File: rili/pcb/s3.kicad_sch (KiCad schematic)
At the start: 91 parts, among them J2 Conn_02x03_Odd_Even, J20 TPS43_FPC, J4 AudioJack4, SW100 SW_PUSH, SW101 SW_PUSH, SW102 SW_PUSH, SW103 SW_PUSH, SW104 SW_PUSH, SW105 SW_PUSH, SW74 SW_PUSH, SW75 SW_PUSH, SW76 SW_PUSH, SW77 SW_PUSH, SW82 SW_PUSH, SW83 SW_PUSH, SW84 SW_PUSH, SW85 SW_PUSH, SW88 SW_PUSH, SW89 SW_PUSH, SW90 SW_PUSH, SW91 SW_PUSH, SW92 SW_PUSH, SW93 SW_PUSH, SW94 SW_PUSH, SW95 SW_PUSH, SW96 SW_PUSH, SW97 SW_PUSH, SW98 SW_PUSH, SW99 SW_PUSH, U1 ESP32-S3-WROOM-1, U10 SiP32431DR3, U13 D, U14 D, U8 NRF24L01_Breakout, U9 SRV05-4

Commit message: layout v2 : carte routée — PCB↔schéma réconciliés, BOM LCSC, TVS matrice, DRC 990→24
- réconciliation PCB↔schéma en une passe : 105 empreintes remariées (matrice ×2,
  module P4), 54 périmées supprimées, ~140 importées par F8 ; footprint TRRS
  MJ-4PP-9_rev3 créé (pads mappés de l'ancien design fonctionnel)
- placement : moitié droite générée au miroir exact du pré-placement gauche
  (axe x=188.46048), trous de montage symétrisés, origine de grille sur l'axe
- protection ESD matrice : 22 SD05C-01F (un par ligne, côté switchs des 100R,
  validés par partition de netlist) ; PWR_FLAG +5V_D réparé
- BOM LCSC dans les propriétés des symboles (32 composants : réfs, liens,
  notes d'achat) + annexe courses complète au plan v2 ; connecteur trackpad
  corrigé (ZIF Hirose FH12-6S-0.5SH, réf MNT Reform)
- règles JLCPCB (planchers DRC + classes Default/Power re-branchées v2),
  passage 4 couches, routage complet des deux moitiés
- gerbers v1 corne-cherry retirés (obsolètes)
- baselines tripwire re-référencées : DRC 990→24 erreurs / 208→17 warnings,
  ERC 0 erreur / 200 warnings (53 fantômes headless documentés)

Co-Authored-By: Claude Fable 5 <noreply@anthropic.com>
Claude-Session: https://claude.ai/code/session_01GfX5RmekmQi78Dm37qsT4Z
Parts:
- added D100, D101, D102, D103, D104, D105, D106, D107, D108, D109, D110: SD05C-01F, Diode_SMD:D_SOD-323, symbol Diode:SD05C-01F
- added H5, H6, H7, H8: MountingHole_Pad_MP, MountingHole:MountingHole_3.2mm_M3_DIN965_Pad, symbol Mechanical:MountingHole_Pad_MP
- added J12: Conn_01x05_Pin, Connector_PinHeader_2.54mm:PinHeader_1x05_P2.54mm_Vertical, symbol Connector:Conn_01x05_Pin
- D11: renamed from D78; footprint EKR82-footprint:Diode_TH_SOD123EKR -> Diode_SMD:D_SOD-123
- D13: renamed from D79; footprint EKR82-footprint:Diode_TH_SOD123EKR -> Diode_SMD:D_SOD-123
- D16: renamed from D82; footprint EKR82-footprint:Diode_TH_SOD123EKR -> Diode_SMD:D_SOD-123
- D18: renamed from D83; footprint EKR82-footprint:Diode_TH_SOD123EKR -> Diode_SMD:D_SOD-123
- D2: renamed from D69; footprint EKR82-footprint:Diode_TH_SOD123EKR -> Diode_SMD:D_SOD-123
- D20: renamed from D84; footprint EKR82-footprint:Diode_TH_SOD123EKR -> Diode_SMD:D_SOD-123
- D21: renamed from D85; footprint EKR82-footprint:Diode_TH_SOD123EKR -> Diode_SMD:D_SOD-123
- D24: renamed from D86; footprint EKR82-footprint:Diode_TH_SOD123EKR -> Diode_SMD:D_SOD-123
- D26: renamed from D87; footprint EKR82-footprint:Diode_TH_SOD123EKR -> Diode_SMD:D_SOD-123
- D28: renamed from D88; footprint EKR82-footprint:Diode_TH_SOD123EKR -> Diode_SMD:D_SOD-123
- D3: renamed from D70; footprint EKR82-footprint:Diode_TH_SOD123EKR -> Diode_SMD:D_SOD-123
- D30: renamed from D89; footprint EKR82-footprint:Diode_TH_SOD123EKR -> Diode_SMD:D_SOD-123
- D32: renamed from D90; footprint EKR82-footprint:Diode_TH_SOD123EKR -> Diode_SMD:D_SOD-123
- D33: renamed from D91; footprint EKR82-footprint:Diode_TH_SOD123EKR -> Diode_SMD:D_SOD-123
- D36: renamed from D92; footprint EKR82-footprint:Diode_TH_SOD123EKR -> Diode_SMD:D_SOD-123
- D38: renamed from D93; footprint EKR82-footprint:Diode_TH_SOD123EKR -> Diode_SMD:D_SOD-123
- D40: renamed from D94; footprint EKR82-footprint:Diode_TH_SOD123EKR -> Diode_SMD:D_SOD-123
- D41: renamed from D95; footprint EKR82-footprint:Diode_TH_SOD123EKR -> Diode_SMD:D_SOD-123
- D43: renamed from D96; footprint EKR82-footprint:Diode_TH_SOD123EKR -> Diode_SMD:D_SOD-123
- D46: renamed from D97; footprint EKR82-footprint:Diode_TH_SOD123EKR -> Diode_SMD:D_SOD-123
- D48: renamed from D98; footprint EKR82-footprint:Diode_TH_SOD123EKR -> Diode_SMD:D_SOD-123
- D6: renamed from D71; footprint EKR82-footprint:Diode_TH_SOD123EKR -> Diode_SMD:D_SOD-123
- D8: renamed from D72; footprint EKR82-footprint:Diode_TH_SOD123EKR -> Diode_SMD:D_SOD-123
- D9: renamed from D77; footprint EKR82-footprint:Diode_TH_SOD123EKR -> Diode_SMD:D_SOD-123
- J3: renamed from J20; footprint Connector_PinHeader_2.54mm:PinHeader_1x06_P2.54mm_Vertical -> Connector_FFC-FPC:Hirose_FH12-6S-0.5SH_1x06-1MP_P0.50mm_Horizontal; LCSC (none) -> C202118; Lien (none) -> https://lcsc.com/product-detail/C202118.html; Note achat (none) -> Hirose FH12-6S-0.5SH — ZIF 6P 0,5mm contacts bas ; nappe FF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
- J6: renamed from J4; footprint (none) -> EKR82-footprint:MJ-4PP-9_rev3; Achat (none) -> jack TRRS MJ-4PP-9 AliExpress; Lien (none) -> https://fr.aliexpress.com/item/33029465106.html
- SW1: renamed from SW74; footprint PMW3360:SW_Hotswap_Kailh_Choc_V1V2_1.00u -> key:SW_Cherry_MX_1.00u_PCB
- SW10: renamed from SW82; footprint PMW3360:SW_Hotswap_Kailh_Choc_V1V2_1.00u -> key:SW_Cherry_MX_1.00u_PCB
- SW12: renamed from SW83; footprint PMW3360:SW_Hotswap_Kailh_Choc_V1V2_1.00u -> key:SW_Cherry_MX_1.00u_PCB
- SW14: renamed from SW84; footprint PMW3360:SW_Hotswap_Kailh_Choc_V1V2_1.00u -> key:SW_Cherry_MX_1.00u_PCB
- SW15: renamed from SW85; footprint PMW3360:SW_Hotswap_Kailh_Choc_V1V2_1.00u -> key:SW_Cherry_MX_1.00u_PCB
- SW17: renamed from SW88; footprint PMW3360:SW_Hotswap_Kailh_Choc_V1V2_1.00u -> key:SW_Cherry_MX_1.00u_PCB
- SW19: renamed from SW89; footprint PMW3360:SW_Hotswap_Kailh_Choc_V1V2_1.00u -> key:SW_Cherry_MX_1.00u_PCB
- SW21: renamed from SW90; footprint PMW3360:SW_Hotswap_Kailh_Choc_V1V2_1.00u -> key:SW_Cherry_MX_1.00u_PCB
- SW24: renamed from SW91; footprint PMW3360:SW_Hotswap_Kailh_Choc_V1V2_1.00u -> key:SW_Cherry_MX_1.00u_PCB
- SW26: renamed from SW92; footprint PMW3360:SW_Hotswap_Kailh_Choc_V1V2_1.00u -> key:SW_Cherry_MX_1.00u_PCB
- SW27: renamed from SW93; footprint PMW3360:SW_Hotswap_Kailh_Choc_V1V2_1.00u -> key:SW_Cherry_MX_1.00u_PCB
- SW3: renamed from SW75; footprint PMW3360:SW_Hotswap_Kailh_Choc_V1V2_1.00u -> key:SW_Cherry_MX_1.00u_PCB
- SW30: renamed from SW94; footprint PMW3360:SW_Hotswap_Kailh_Choc_V1V2_1.00u -> key:SW_Cherry_MX_1.00u_PCB
- SW31: renamed from SW95; footprint PMW3360:SW_Hotswap_Kailh_Choc_V1V2_1.00u -> key:SW_Cherry_MX_1.00u_PCB
- SW33: renamed from SW96; footprint PMW3360:SW_Hotswap_Kailh_Choc_V1V2_1.00u -> key:SW_Cherry_MX_1.00u_PCB
- SW35: renamed from SW97; footprint PMW3360:SW_Hotswap_Kailh_Choc_V1V2_1.00u -> key:SW_Cherry_MX_1.00u_PCB
- SW38: renamed from SW98; footprint PMW3360:SW_Hotswap_Kailh_Choc_V1V2_1.00u -> key:SW_Cherry_MX_1.00u_PCB
- SW40: renamed from SW99; footprint PMW3360:SW_Hotswap_Kailh_Choc_V1V2_1.00u -> key:SW_Cherry_MX_1.00u_PCB
- SW41: renamed from SW100; footprint PMW3360:SW_Hotswap_Kailh_Choc_V1V2_1.00u -> key:SW_Cherry_MX_1.00u_PCB
- SW43: renamed from SW101; footprint PMW3360:SW_Hotswap_Kailh_Choc_V1V2_1.00u -> key:SW_Cherry_MX_1.00u_PCB
- SW45: renamed from SW102; footprint PMW3360:SW_Hotswap_Kailh_Choc_V1V2_1.00u -> key:SW_Cherry_MX_1.00u_PCB
- SW47: renamed from SW103; footprint PMW3360:SW_Hotswap_Kailh_Choc_V1V2_1.00u -> key:SW_Cherry_MX_1.00u_PCB
- SW49: renamed from SW104; footprint PMW3360:SW_Hotswap_Kailh_Choc_V1V2_1.00u -> key:SW_Cherry_MX_1.00u_PCB
- SW5: renamed from SW76; footprint PMW3360:SW_Hotswap_Kailh_Choc_V1V2_1.00u -> key:SW_Cherry_MX_1.00u_PCB
- SW52: renamed from SW105; footprint PMW3360:SW_Hotswap_Kailh_Choc_V1V2_1.00u -> key:SW_Cherry_MX_1.00u_PCB
- SW8: renamed from SW77; footprint PMW3360:SW_Hotswap_Kailh_Choc_V1V2_1.00u -> key:SW_Cherry_MX_1.00u_PCB
- U12: renamed from U10; LCSC (none) -> C141606; Lien (none) -> https://lcsc.com/product-detail/C141606.html
- U2: renamed from U13; footprint EKR82-footprint:Diode_TH_SOD123EKR -> Diode_SMD:D_SOD-123
- U3: renamed from U14; footprint EKR82-footprint:Diode_TH_SOD123EKR -> Diode_SMD:D_SOD-123
- U6: renamed from U1; LCSC (none) -> C2913204; Lien (none) -> https://lcsc.com/product-detail/C2913204.html; Note achat (none) -> N8R2 ; si antenne externe (empreinte 1U) : C3013944
- U8: Achat (none) -> module nRF24L01+ AliExpress (2x4 pin)
- U9: LCSC (none) -> C13612; Lien (none) -> https://lcsc.com/product-detail/C13612.html; Note achat (none) -> alt. budget Leiditech C384887
- renumbered C4 to C11, C2 to C3, C21 to C5, C20 to C6, C3 to C8, C5 to C9, J2 to J1, R39 to R11, R40 to R14, R9 to R16, R10 to R18, R8 to R2, R41 to R20, R42 to R21, R43 to R23, R44 to R25, R45 to R27, R50 to R29, R11 to R30, R51 to R32, R12 to R34, R52 to R35, R13 to R36, R14 to R39, R35 to R4, R15 to R41, R22 to R42, R21 to R45, R20 to R47, R36 to R6, R37 to R7, R38 to R9
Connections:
- net +3.3V: now also J12.3 (Pin_3)
- net CS_DPL: now also J12.5 (Pin_5)
- net GND: now also D100.2 (A2), D101.2 (A2), D102.2 (A2), D103.2 (A2), D104.2 (A2), D105.2 (A2), D106.2 (A2), D107.1 (A1), D108.1 (A1), D109.1 (A1), D110.1 (A1), H5.MP, H6.MP, H7.MP, H8.MP, J12.4 (Pin_4)
- net MOSI: now also J12.1 (Pin_1)
- net SCK: now also J12.2 (Pin_2)
- net col0: now also U6.4 (GPIO4/TOUCH4/ADC1_CH3); no longer U6.6 (GPIO6/TOUCH6/ADC1_CH5)
- net col1: now also U6.5 (GPIO5/TOUCH5/ADC1_CH4); no longer U6.7 (GPIO7/TOUCH7/ADC1_CH6)
- net col2: now also U6.7 (GPIO7/TOUCH7/ADC1_CH6); no longer U6.12 (GPIO8/TOUCH8/ADC1_CH7/SUBSPICS1)
- net row2: now also U6.12 (GPIO8/TOUCH8/ADC1_CH7/SUBSPICS1); no longer U6.4 (GPIO4/TOUCH4/ADC1_CH3)
- net row3: now also U6.6 (GPIO6/TOUCH6/ADC1_CH5); no longer U6.5 (GPIO5/TOUCH5/ADC1_CH4)
- net at D11.1 (K), D18.1 (K), D24.1 (K)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: now also D108.2 (A2)
- net at D28.1 (K), D36.1 (K), D43.1 (K)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: now also D110.2 (A2)
- net at R25.1, SW41.1, SW43.1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: now also D105.1 (A1)
- net at R27.1, SW49.1, SW52.1: now also D106.1 (A1)
- net at R11.1, SW1.1, SW3.1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: now also D100.1 (A1)
- net at D13.1 (K), D20.1 (K), D26.1 (K)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: now also D109.2 (A2)
- net at R21.1, SW26.1, SW27.1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: now also D103.1 (A1)
- net at D16.1 (K), D2.1 (K), D21.1 (K)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: now also D107.2 (A2)
- net at R14.1, SW10.1, SW12.1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: now also D101.1 (A1)
- net at R23.1, SW33.1, SW35.1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: now also D104.1 (A1)
- net at R20.1, SW17.1, SW19.1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: now also D102.1 (A1)
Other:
- moved on the sheet: C5, C6, D11, D13, D16, D18, D2, D20, D21, D24, D26, D28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

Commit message: layout : panneau vertical 2 rails dans le dépôt + baseline chantier
Panneau 185×212 (droite tournée 180°, rails + 8 tabs mouse-bites) appliqué par
Mae, F8 des passifs unifiés. Baseline DRC re-référencée 24/19 → 36/26 (état
panneau, finitions DRC prévues : pistes près des lignes de rupture, vias de
maillage orphelins dans les bandes sans cuivre).

Co-Authored-By: Claude Fable 5 <noreply@anthropic.com>
Claude-Session: https://claude.ai/code/session_01GfX5RmekmQi78Dm37qsT4Z
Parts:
- C11, C3, C9: footprint Capacitor_SMD:C_0603_1608Metric -> Capacitor_SMD:C_0805_2012Metric
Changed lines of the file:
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@@
 			)
 		)
-		(property "Footprint" "Capacitor_SMD:C_0603_1608Metric"
+		(property "Footprint" "Capacitor_SMD:C_0805_2012Metric"
 			(at 270.8148 57.15 0)
 			(hide yes)
@@
 			)
 		)
-		(property "Footprint" "Capacitor_SMD:C_0603_1608Metric"
+		(property "Footprint" "Capacitor_SMD:C_0805_2012Metric"
 			(at 269.5448 144.78 0)
 			(hide yes)
@@
 			)
 		)
-		(property "Footprint" "Capacitor_SMD:C_0603_1608Metric"
+		(property "Footprint" "Capacitor_SMD:C_0805_2012Metric"
 			(at 54.9148 33.02 0)
 			(hide yes)

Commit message: review schéma : LDO S3 corrigé (pins SOT-89) + 8 valeurs — HT7833 en place
Revue 4 relecteurs parallèles avant commande, validée ligne à ligne sur la
netlist. BLOQUANT réparé : U20/U21 avaient le brochage SOT-23 du MCP1700 sur
des pastilles SOT-89 → entrée/sortie inversées pour tout LDO réel ; pins 2/3
échangés dans la déf, Value=HT7833 (C50936), F8 + reroutage des 2 zones par
Mae, pads vérifiés (1=GND 2=VIN 3=VOUT). Valeurs : bulk 3V3 C11/C12 et condos
LDO C23-C26 → 10µF (C15850), CHIP_PU P4 R54→10k C14→1µF. Baseline ERC 200→202
(lib_symbol_mismatch des défs LDO éditées). Validé par la revue : chaînes
batterie/charge/load-share, paires USB bout en bout, hub, prog P4 ×2 ports,
microSD IOMUX+pullups, strapping, nRF24, trackpad, 22 TVS matrice.

Co-Authored-By: Claude Fable 5 <noreply@anthropic.com>
Claude-Session: https://claude.ai/code/session_01GfX5RmekmQi78Dm37qsT4Z
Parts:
- C1, C8: footprint Capacitor_SMD:C_0603_1608Metric -> Capacitor_SMD:C_0603_1608Metric_Pad1.08x0.95mm_HandSolder
- C11: value 1uF -> 10uF; footprint Capacitor_SMD:C_0805_2012Metric -> Capacitor_SMD:C_1206_3216Metric_Pad1.33x1.80mm_HandSolder
- C3, C9: footprint Capacitor_SMD:C_0805_2012Metric -> Capacitor_SMD:C_0805_2012Metric_Pad1.18x1.45mm_HandSolder
- R11, R14, R20, R21, R23, R25, R27, R4, R6, R7, R9: value 100R -> 100
- R16, R18, R2, R30, R34, R36, R39, R41: footprint Resistor_SMD:R_0603_1608Metric -> Resistor_SMD:R_0603_1608Metric_Pad0.98x0.95mm_HandSolder
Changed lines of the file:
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@@
 			)
 		)
-		(property "Value" "100R"
+		(property "Value" "100"
 			(at 21.59 405.13 90)
 			(show_name no)
@@
 			)
 		)
-		(property "Value" "100R"
+		(property "Value" "100"
 			(at 147.066 337.82 0)
 			(show_name no)
@@
 			)
 		)
-		(property "Value" "100R"
+		(property "Value" "100"
 			(at 35.306 337.82 0)
 			(show_name no)
@@
 			)
 		)
-		(property "Footprint" "Resistor_SMD:R_0603_1608Metric"
+		(property "Footprint" "Resistor_SMD:R_0603_1608Metric_Pad0.98x0.95mm_HandSolder"
 			(at 227.33 69.088 90)
 			(hide yes)
@@
 			)
 		)
-		(property "Value" "100R"
+		(property "Value" "100"
 			(at 21.59 374.65 90)
 			(show_name no)
@@
 			)
 		)
-		(property "Value" "1uF"
+		(property "Value" "10uF"
 			(at 267.462 58.674 0)
 			(show_name no)
@@
 			)
 		)
-		(property "Footprint" "Capacitor_SMD:C_0805_2012Metric"
+		(property "Footprint" "Capacitor_SMD:C_1206_3216Metric_Pad1.33x1.80mm_HandSolder"
 			(at 270.8148 57.15 0)
 			(hide yes)
@@
 			)
 		)
-		(property "Value" "100R"
+		(property "Value" "100"
 			(at 53.086 337.82 0)
 			(show_name no)
@@
 			)
 		)
-		(property "Footprint" "Capacitor_SMD:C_0805_2012Metric"
+		(property "Footprint" "Capacitor_SMD:C_0805_2012Metric_Pad1.18x1.45mm_HandSolder"
 			(at 269.5448 144.78 0)
 			(hide yes)
@@
 			)
 		)
-		(property "Footprint" "Resistor_SMD:R_0603_1608Metric"
+		(property "Footprint" "Resistor_SMD:R_0603_1608Metric_Pad0.98x0.95mm_HandSolder"
 			(at 34.29 34.798 90)
 			(hide yes)
@@
 			)
 		)
-		(property "Value" "100R"
+		(property "Value" "100"
 			(at 88.646 337.566 0)
 			(show_name no)
@@
 			)
 		)
-		(property "Value" "100R"
+		(property "Value" "100"
 			(at 105.918 337.566 0)
 			(show_name no)
@@
 			)
 		)
-		(property "Footprint" "Capacitor_SMD:C_0603_1608Metric"
+		(property "Footprint" "Capacitor_SMD:C_0603_1608Metric_Pad1.08x0.95mm_HandSolder"
 			(at 44.7548 33.02 0)
 			(hide yes)
@@
 			)
 		)
-		(property "Footprint" "Resistor_SMD:R_0603_1608Metric"
+		(property "Footprint" "Resistor_SMD:R_0603_1608Metric_Pad0.98x0.95mm_HandSolder"
 			(at 181.61 95.758 90)
 			(hide yes)
@@
 			)
 		)
-		(property "Footprint" "Capacitor_SMD:C_0805_2012Metric"
+		(property "Footprint" "Capacitor_SMD:C_0805_2012Metric_Pad1.18x1.45mm_HandSolder"
 			(at 54.9148 33.02 0)
 			(hide yes)
@@
 			)
 		)
-		(property "Footprint" "Capacitor_SMD:C_0603_1608Metric"
+		(property "Footprint" "Capacitor_SMD:C_0603_1608Metric_Pad1.08x0.95mm_HandSolder"
 			(at 260.6548 57.15 0)
 			(hide yes)
@@
 			)
 		)
-		(property "Value" "100R"
+		(property "Value" "100"
 			(at 21.59 389.89 90)
 			(show_name no)
@@
 			)
 		)
-		(property "Value" "100R"
+		(property "Value" "100"
 			(at 70.866 337.82 0)
 			(show_name no)
@@
 			)
 		)
-		(property "Value" "100R"
+		(property "Value" "100"
 			(at 123.952 338.074 0)
 			(show_name no)
@@
 			)
 		)
-		(property "Footprint" "Resistor_SMD:R_0603_1608Metric"
+		(property "Footprint" "Resistor_SMD:R_0603_1608Metric_Pad0.98x0.95mm_HandSolder"
 			(at 227.33 76.708 90)
 			(hide yes)
@@
 			)
 		)
-		(property "Footprint" "Resistor_SMD:R_0603_1608Metric"
+		(property "Footprint" "Resistor_SMD:R_0603_1608Metric_Pad0.98x0.95mm_HandSolder"
 			(at 72.39 46.482 90)
 			(hide yes)
@@
 			)
 		)
-		(property "Footprint" "Resistor_SMD:R_0603_1608Metric"
+		(property "Footprint" "Resistor_SMD:R_0603_1608Metric_Pad0.98x0.95mm_HandSolder"
 			(at 198.12 52.578 90)
 			(hide yes)
@@
 			)
 		)
-		(property "Footprint" "Resistor_SMD:R_0603_1608Metric"
+		(property "Footprint" "Resistor_SMD:R_0603_1608Metric_Pad0.98x0.95mm_HandSolder"
 			(at 227.33 74.168 90)
 			(hide yes)
@@
 			)
 		)
-		(property "Footprint" "Resistor_SMD:R_0603_1608Metric"
+		(property "Footprint" "Resistor_SMD:R_0603_1608Metric_Pad0.98x0.95mm_HandSolder"
 			(at 72.39 49.022 90)
 			(hide yes)
@@
 			)
 		)
-		(property "Value" "100R"
+		(property "Value" "100"
 			(at 21.59 359.41 90)
 			(show_name no)

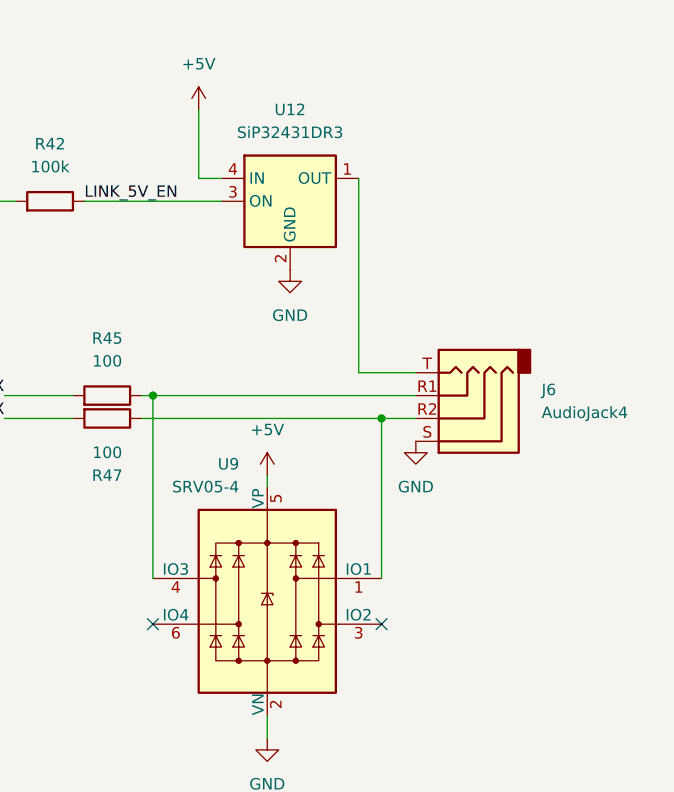
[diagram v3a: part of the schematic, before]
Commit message: review : solde complet — Tip TRRS protégé, condos +BATT, prog P4 dégagée
- TVS Tip : canal 3 des SRV05 relié au Tip des deux jacks (net TIP_5V, validé
  netlist : jack.T + load switch OUT + SRV05 sans toucher LINK_5V_EN)
- C29/C30 : 10µF sur +BATT/+BATT_D près des TP4056, placés et routés par Mae
- R48/R49 supprimés par Mae (CH334R : pull-up RESET# interne 25k, mode
  sans-quartz XO flottant conforme datasheet, fuite batterie→hub éliminée)
- pistes JP1/JP2 (prog USB du P4) écartées de la zone GND : zéro violation
- nettoyage : no_connect orpheline de la dépose R48/R49
- DRC 36/26 → 17/22 (ménage de routage par Mae), ratchet enregistré

Décisions documentées : SD manipulée hors tension (pas de TVS SD), tables de
pins matrice réelles + conventions firmware en annexe du plan v2.

Co-Authored-By: Claude Fable 5 <noreply@anthropic.com>
Claude-Session: https://claude.ai/code/session_01GfX5RmekmQi78Dm37qsT4Z
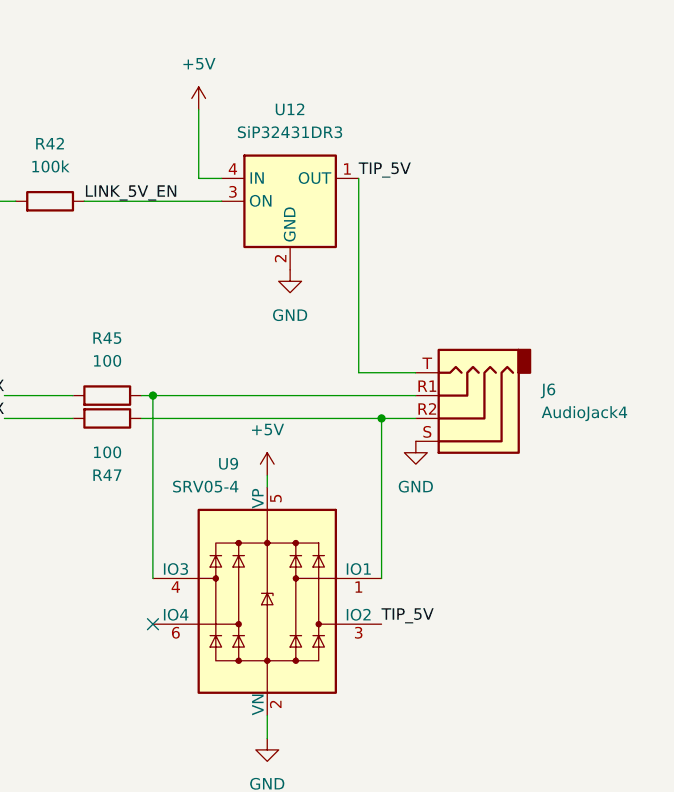
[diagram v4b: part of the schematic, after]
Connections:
- net TIP_5V: now reaches U9.3 (IO2)
- net TIP_5V: now also J6.T, U12.1 (OUT)
- no-connect marks 8 -> 7
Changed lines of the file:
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@@
-	)
-	(no_connect
-		(at 364.49 86.36)
 	)
 	(no_connect
@@
 		)
 	)
+	(label "TIP_5V"
+		(at 361.95 36.83 0)
+		(effects
+			(font
+				(size 1.27 1.27)
+			)
+			(justify left bottom)
+		)
+	)
 	(label "row0"
 		(at 11.43 363.22 0)
@@
 		(effects
 			(font
+				(size 1.27 1.27)
+			)
+			(justify left bottom)
+		)
+	)
+	(label "TIP_5V"
+		(at 364.49 86.36 0)
+		(effects
+			(font
